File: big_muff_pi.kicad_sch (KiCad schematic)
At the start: 78 parts, among them J1 NMJ6HHD2, J2 NMJ6HHD2, J3 Conn_01x05, J4 Conn_01x05, J5 Conn_01x05, J6 Barrel_Jack_MountingPin, P1 big_muff_pi_front_panel, Q1 MMBT5551, Q2 MMBT5551, Q3 MMBT5551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

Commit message: Lib sync.
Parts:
- removed SW1: SW_DPDT_x2, switch:switch_DPDT, symbol Switch:SW_DPDT_x2
- added SW1: pedala_switch, pedale:switch_DPDT, symbol pedale:pedala_switch
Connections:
- net 9V: now also SW1.4 (A)
- net SW_IN: now also SW1.3 (C)
- net at J5.2 (Pin_2): now also SW1.1 (A)
- net at J2.T: now also SW1.2 (B)
- net at J5.4 (Pin_4): now also SW1.5 (B)
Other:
- note added: "BAKAR U FRONT PLATE-u KAO UKRAS FARADEJEV KAVEZ~"
- note added: "DOUBLE CHECK SWITCH"
- note added: "MOŽDA DODAJ ŠRAFOVE I SA STRANE, BOLJA ROBUSTNOST"
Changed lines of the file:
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@@
 		)
 	)
+	(text "MOŽDA DODAJ ŠRAFOVE I SA STRANE, BOLJA ROBUSTNOST\n"
+		(exclude_from_sim no)
+		(at 121.666 117.856 0)
+		(effects
+			(font
+				(size 5.08 5.08)
+				(color 255 0 0 1)
+			)
+		)
+	)
+	(text "BAKAR U FRONT PLATE-u KAO UKRAS\nFARADEJEV KAVEZ~"
+		(exclude_from_sim no)
+		(at 112.014 148.59 0)
+		(effects
+			(font
+				(size 5.08 5.08)
+				(color 255 0 0 1)
+			)
+		)
+	)
 	(text "Mounting and estetics"
 		(exclude_from_sim no)
@@
 		)
 	)
+	(text "DOUBLE CHECK SWITCH"
+		(exclude_from_sim no)
+		(at 124.206 101.092 0)
+		(effects
+			(font
+				(size 5.08 5.08)
+				(color 255 0 0 1)
+			)
+		)
+	)
 	(junction
 		(at 232.41 48.895)
@@
 	)
 	(symbol
+		(lib_id "pedale:pedala_switch")
+		(at 222.25 110.49 0)
+		(unit 2)
+		(exclude_from_sim no)
+		(in_bom yes)
+		(on_board yes)
+		(dnp no)
+		(fields_autoplaced yes)
+		(property "Reference" "SW1"
+			(at 222.25 101.6 0)
+			(effects
+				(font
+					(size 1.27 1.27)
+				)
+			)
+		)
+		(property "Value" "pedala_switch"
+			(at 222.25 104.14 0)
+			(effects
+				(font
+					(size 1.27 1.27)
+				)
+			)
+		)
+		(property "Footprint" "pedale:switch_DPDT"
+			(at 222.25 110.49 0)
+			(effects
+				(font
+					(size 1.27 1.27)
+				)
+				(hide yes)
+			)
+		)
+		(property "Datasheet" "~"
+			(at 222.25 110.49 0)
+			(effects
+				(font
+					(size 1.27 1.27)
+				)
+				(hide yes)
+			)
+		)
+		(property "Description" "Switch, dual pole double throw, separate symbols"
+			(at 222.25 110.49 0)
+			(effects
+				(font
+					(size 1.27 1.27)
+				)
+				(hide yes)
+			)
+		)
+		(pin "2"
+		)
+		(pin "1"
+		)
+		(pin "3"
+		)
+		(pin "6"
+		)
+		(pin "4"
+		)
+		(pin "5"
+		)
+		(instances
+			(project ""
+				(path "/1fda0e48-ac05-4486-b24b-352a2425b266"
+					(reference "SW1")
+					(unit 2)
+				)
+			)
+		)
+	)
+	(symbol
 		(lib_id "pedale:floating_pot")
 		(at 238.125 34.29 0)
@@
 	)
 	(symbol
+		(lib_id "pedale:pedala_switch")
+		(at 222.25 127 0)
+		(mirror y)
+		(unit 1)
+		(exclude_from_sim no)
+		(in_bom yes)
+		(on_board yes)
+		(dnp no)
+		(fields_autoplaced yes)
+		(property "Reference" "SW1"
+			(at 222.25 118.11 0)
+			(effects
+				(font
+					(size 1.27 1.27)
+				)
+			)
+		)
+		(property "Value" "pedala_switch"
+			(at 222.25 120.65 0)
+			(effects
+				(font
+					(size 1.27 1.27)
+				)
+			)
+		)
+		(property "Footprint" "pedale:switch_DPDT"
+			(at 222.25 127 0)
+			(effects
+				(font
+					(size 1.27 1.27)
+				)
+				(hide yes)
+			)
+		)
+		(property "Datasheet" "~"
+			(at 222.25 127 0)
+			(effects
+				(font
+					(size 1.27 1.27)
+				)
+				(hide yes)
+			)
+		)
+		(property "Description" "Switch, dual pole double throw, separate symbols"
+			(at 222.25 127 0)
+			(effects
+				(font
+					(size 1.27 1.27)
+				)
+				(hide yes)
+			)
+		)
+		(pin "2"
+		)
+		(pin "1"
+		)
+		(pin "3"
+		)
+		(pin "6"
+		)
+		(pin "4"
+		)
+		(pin "5"
+		)
+		(instances
+			(project ""
+				(path "/1fda0e48-ac05-4486-b24b-352a2425b266"
+					(reference "SW1")
+					(unit 1)
+				)
+			)
+		)
+	)
+	(symbol
 		(lib_id "Device:R")
 		(at 172.72 104.14 180)
@@
 	)
 	(symbol
-		(lib_id "Switch:SW_DPDT_x2")
-		(at 222.25 127 0)
-		(mirror y)
-		(unit 1)
-		(exclude_from_sim no)
-		(in_bom yes)
-		(on_board yes)
-		(dnp no)
-		(property "Reference" "SW1"
-			(at 222.25 118.11 0)
-			(effects
-				(font
-					(size 1.27 1.27)
-				)
-			)
-		)
-		(property "Value" "SW_DPDT_x2"
-			(at 222.25 120.65 0)
-			(effects
-				(font
-					(size 1.27 1.27)
-				)
-			)
-		)
-		(property "Footprint" "switch:switch_DPDT"
-			(at 222.25 127 0)
-			(effects
-				(font
-					(size 1.27 1.27)
-				)
-				(hide yes)
-			)
-		)
-		(property "Datasheet" "~"
-			(at 222.25 127 0)
-			(effects
-				(font
-					(size 1.27 1.27)
-				)
-				(hide yes)
-			)
-		)
-		(property "Description" "Switch, dual pole double throw, separate symbols"
-			(at 222.25 127 0)
-			(effects
-				(font
-					(size 1.27 1.27)
-				)
-				(hide yes)
-			)
-		)
-		(pin "3"
-		)
-		(pin "6"
-		)
-		(pin "5"
-		)
-		(pin "2"
-		)
-		(pin "1"
-		)
-		(pin "4"
-		)
-		(instances
-			(project "big_muff_pi"
-				(path "/1fda0e48-ac05-4486-b24b-352a2425b266"
-					(reference "SW1")
-					(unit 1)
-				)
-			)
-		)
-	)
-	(symbol
 		(lib_id "pedale:floating_pot")
 		(at 130.175 33.02 90)
@@
 				)
 			)
-		)
-	)
-	(symbol
-		(lib_id "Switch:SW_DPDT_x2")
-		(at 222.25 110.49 0)
-		(unit 2)
-		(exclude_from_sim no)
-		(in_bom yes)
-		(on_board yes)
-		(dnp no)
-		(property "Reference" "SW1"
-			(at 222.25 101.6 0)
-			(effects
-				(font
-					(size 1.27 1.27)
-				)
-			)
-		)
-		(property "Value" "SW_DPDT_x2"
-			(at 222.25 104.14 0)
-			(effects
-				(font
-					(size 1.27 1.27)
-				)
-			)
-		)
-		(property "Footprint" "switch:switch_DPDT"
-			(at 222.25 110.49 0)
-			(effects
-				(font
-					(size 1.27 1.27)
-				)
-				(hide yes)
-			)
-		)
-		(property "Datasheet" "~"
-			(at 222.25 110.49 0)
-			(effects
-				(font
-					(size 1.27 1.27)
-				)
-				(hide yes)
-			)
-		)
-		(property "Description" "Switch, dual pole double throw, separate symbols"
-			(at 222.25 110.49 0)
-			(effects
-				(font
-					(size 1.27 1.27)
-				)
-				(hide yes)
-			)
-		)
-		(pin "3"
-		)
-		(pin "6"
-		)
-		(pin "5"
-		)
-		(pin "2"
-		)
-		(pin "1"
-		)
-		(pin "4"
-		)
-		(instances
-			(project "big_muff_pi"
-				(path "/1fda0e48-ac05-4486-b24b-352a2425b266"
-					(reference "SW1")
-					(unit 2)
-				)
-			)

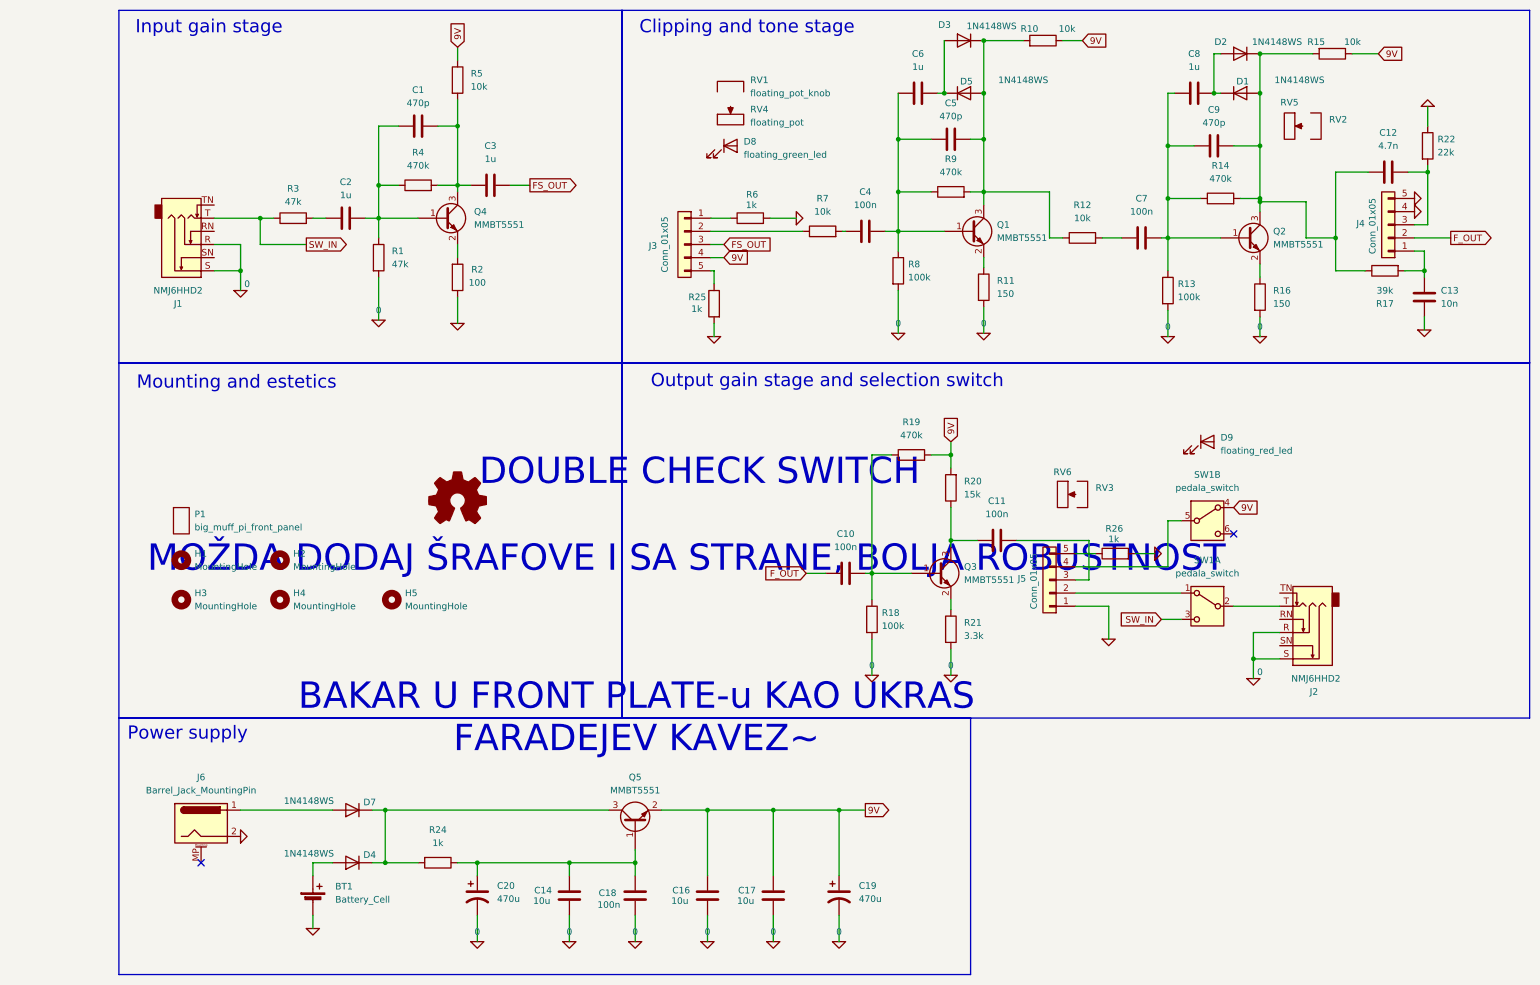
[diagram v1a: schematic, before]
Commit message: New switch
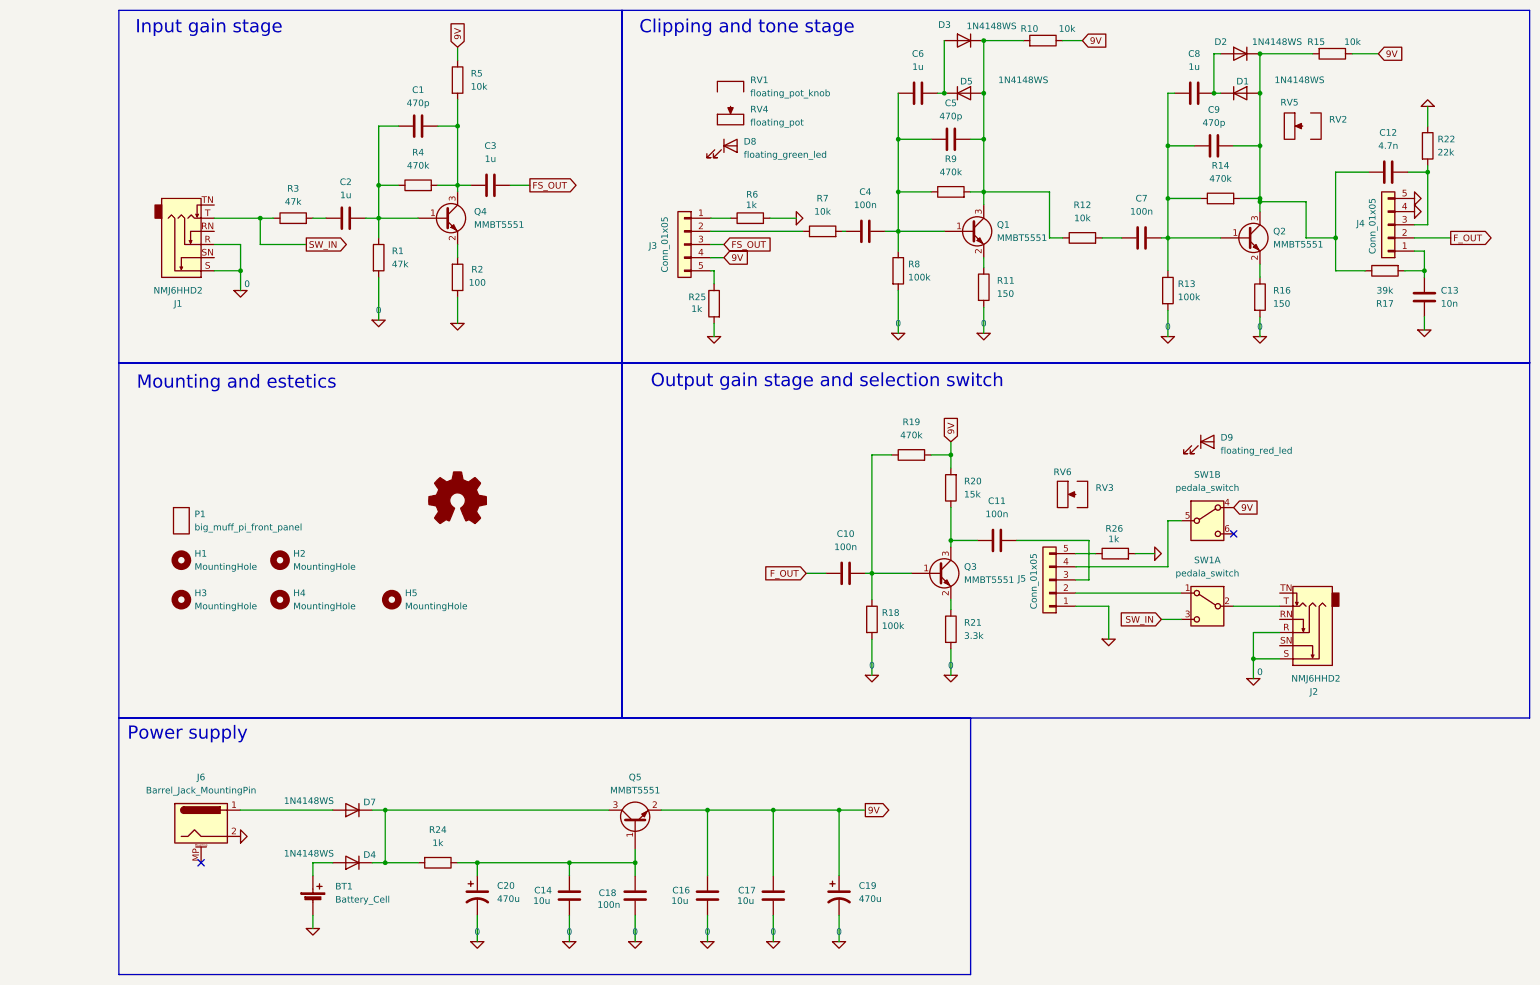
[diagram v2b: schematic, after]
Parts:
- SW1: footprint pedale:switch_DPDT -> pedale:foot_switch
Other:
- note removed: "BAKAR U FRONT PLATE-u KAO UKRAS FARADEJEV KAVEZ~"
- note removed: "DOUBLE CHECK SWITCH"
- note removed: "MOŽDA DODAJ ŠRAFOVE I SA STRANE, BOLJA ROBUSTNOST"
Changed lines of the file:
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@@
 		)
 	)
-	(text "MOŽDA DODAJ ŠRAFOVE I SA STRANE, BOLJA ROBUSTNOST\n"
-		(exclude_from_sim no)
-		(at 121.666 117.856 0)
-		(effects
-			(font
-				(size 5.08 5.08)
-				(color 255 0 0 1)
-			)
-		)
-	)
-	(text "BAKAR U FRONT PLATE-u KAO UKRAS\nFARADEJEV KAVEZ~"
-		(exclude_from_sim no)
-		(at 112.014 148.59 0)
-		(effects
-			(font
-				(size 5.08 5.08)
-				(color 255 0 0 1)
-			)
-		)
-	)
 	(text "Mounting and estetics"
 		(exclude_from_sim no)
@@
 		)
 	)
-	(text "DOUBLE CHECK SWITCH"
-		(exclude_from_sim no)
-		(at 124.206 101.092 0)
-		(effects
-			(font
-				(size 5.08 5.08)
-				(color 255 0 0 1)
-			)
-		)
-	)
 	(junction
 		(at 232.41 48.895)
@@
 			)
 		)
-		(property "Footprint" "pedale:switch_DPDT"
+		(property "Footprint" "pedale:foot_switch"
 			(at 222.25 110.49 0)
 			(effects
@@
 			)
 		)
-		(property "Footprint" "pedale:switch_DPDT"
+		(property "Footprint" "pedale:foot_switch"
 			(at 222.25 127 0)
 			(effects

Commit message: Updated library.
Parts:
- removed J1, J2: NMJ6HHD2, Connector_Audio:Jack_6.35mm_Neutrik_NMJ6HHD2_Horizontal, symbol Connector_Audio:NMJ6HHD2
- removed J6: Barrel_Jack_MountingPin, Connector_BarrelJack:BarrelJack_GCT_DCJ200-10-A_Horizontal, symbol Connector:Barrel_Jack_MountingPin
- removed RV1, RV2, RV3: floating_pot_knob, pedale:floating_pot_knob, symbol pedale:floating_pot_knob
- added J1, J2: Jack_6.35, pedale:Jack_6.35mm, symbol pedale:Jack_6.35
- added J7, J8: Conn_01x01_Socket, TestPoint:TestPoint_THTPad_D2.5mm_Drill1.2mm, symbol Connector:Conn_01x01_Socket
- added J9: Barrel_Jack_Switch, pedale:BarrelJack, symbol Connector:Barrel_Jack_Switch
- SW1: footprint pedale:foot_switch -> pedale:foot_switch_tht_and_floating
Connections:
- net 0: now also J1.R, J1.S, J2.R, J2.S, J9.2; no longer BT1.2 (-)
- net SW_IN: now also J1.T
- net at BT1.1 (+), D4.2 (A): now also J7.1 (Pin_1)
- net at SW1.2 (B): now also J2.T
- net at D7.2 (A): now also J9.1
- new net: BT1.2 (-), J8.1 (Pin_1), J9.3
- no-connect marks 2 -> 1

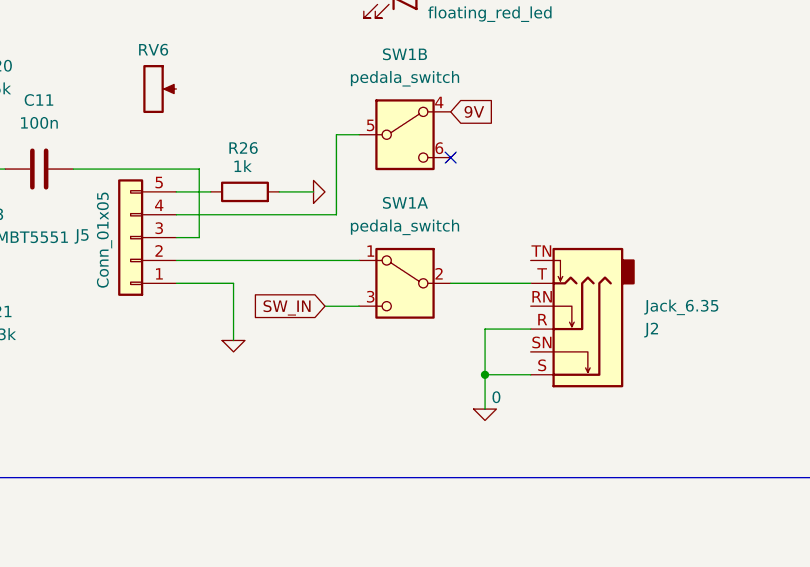
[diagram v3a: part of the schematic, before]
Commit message: Rotated 6.35 pins, switched connector positions, switched LED.
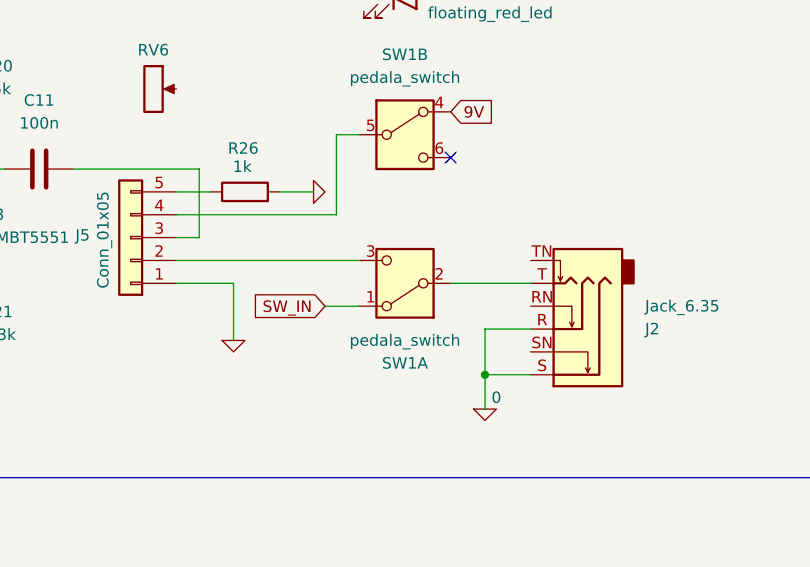
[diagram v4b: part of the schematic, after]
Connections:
- net SW_IN: now also SW1.1 (A); no longer SW1.3 (C)
- net at J5.2 (Pin_2): now also SW1.3 (C); no longer SW1.1 (A)
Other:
- moved on the sheet: SW1A
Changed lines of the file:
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@@
 	(symbol
 		(lib_id "pedale:pedala_switch")
-		(at 222.25 127 0)
-		(mirror y)
+		(at 222.25 127 180)
 		(unit 1)
 		(exclude_from_sim no)
@@
 		(on_board yes)
 		(dnp no)
-		(fields_autoplaced yes)
 		(property "Reference" "SW1"
-			(at 222.25 118.11 0)
+			(at 222.25 135.89 0)
 			(effects
 				(font
@@
 		)
 		(property "Value" "pedala_switch"
-			(at 222.25 120.65 0)
+			(at 222.25 133.35 0)
 			(effects
 				(font
